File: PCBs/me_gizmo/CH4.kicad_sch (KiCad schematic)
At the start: 10 parts, among them J4 PushButton_Terminal_01x06, U1 ADG714, U3 ADG714, U4 ADG714

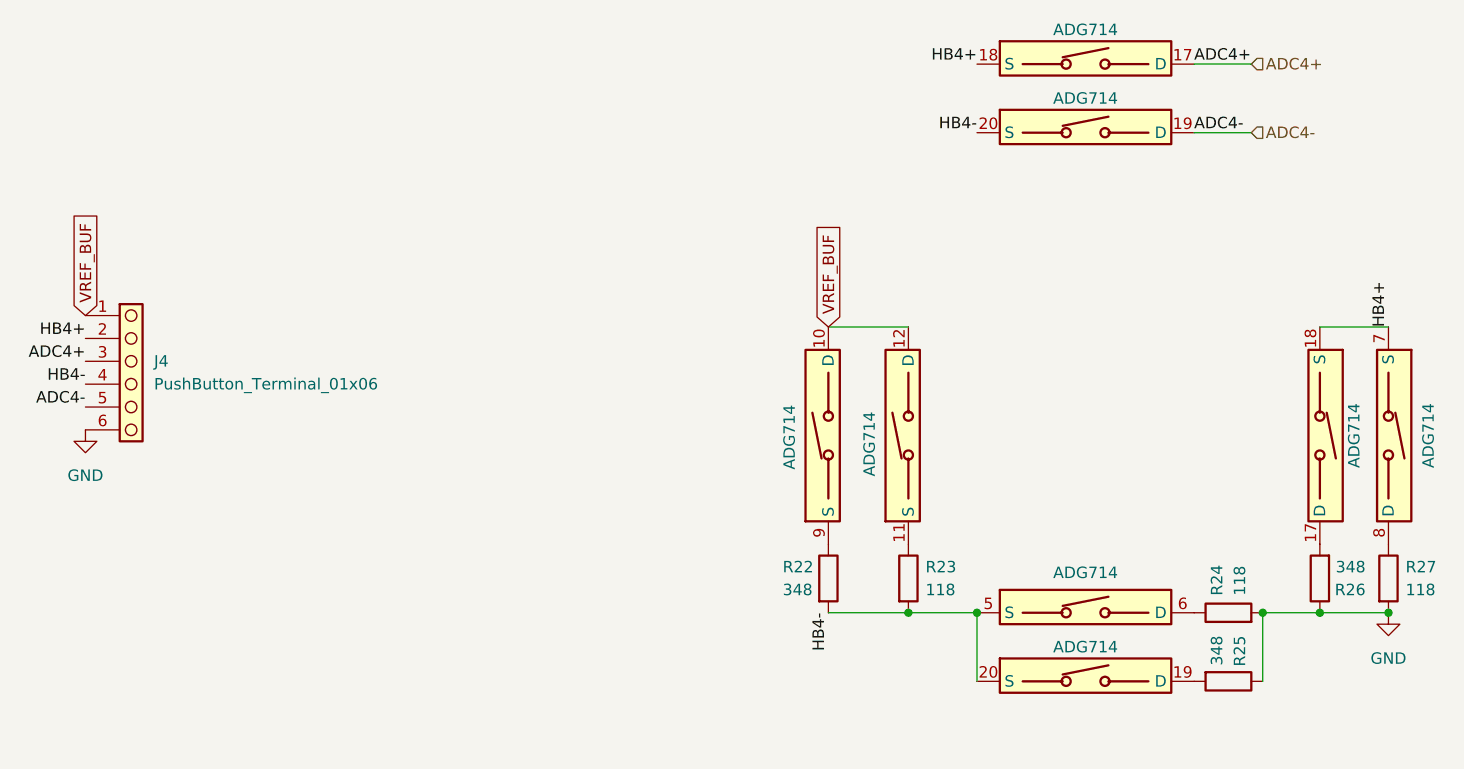
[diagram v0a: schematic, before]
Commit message: Completed first draft of integrated measurement unit
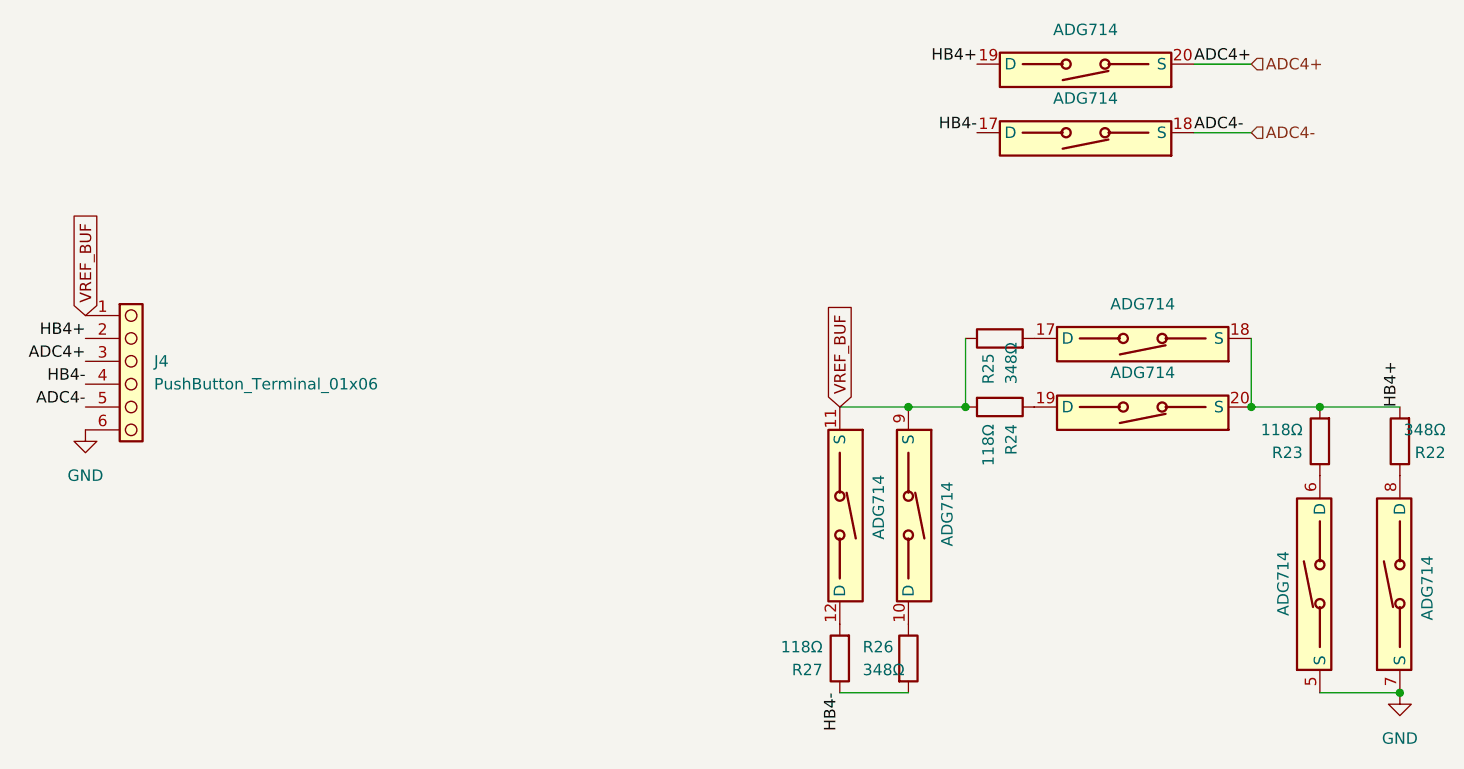
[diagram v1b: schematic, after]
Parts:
- J4: footprint WAGO:CONN5_233-505_WAG -> TerminalBlock_WAGO:TerminalBlock_WAGO_233-506_2x06_P2.54mm
- R22, R25, R26: value 348 -> 348Ω
- R23, R24, R27: value 118 -> 118Ω
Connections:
- net ADC4+: now also U3.20 (S); no longer U3.17 (D)
- net ADC4-: now also U3.18 (S); no longer U3.19 (D)
- net GND: now also U4.5 (S), U4.7 (S); no longer R24.2, R25.1, R26.1, R27.2
- net HB4+: now also R22.2, R23.2, U3.19 (D), U4.20 (S); no longer U3.18 (S), U4.7 (S)
- net HB4-: now also R26.2, R27.1, U3.17 (D); no longer R22.2, R23.2, U3.20 (S), U4.20 (S), U4.5 (S)
- net VREF_BUF: now also R24.2, R25.1, U1.11 (S), U1.9 (S); no longer U1.10 (D), U1.12 (D)
- net at U4.19 (D): now also R24.1; no longer R25.2
- net at U4.6 (D): now also R23.1; no longer R24.1
- net at U4.17 (D): now also R25.2; no longer R26.2
- net at R22.1: now also U4.8 (D); no longer U1.9 (S)
- new net: R26.1, U1.10 (D)
- new net: R27.2, U1.12 (D)
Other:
- moved on the sheet: R22, R23, R24, R25, R26, R27
